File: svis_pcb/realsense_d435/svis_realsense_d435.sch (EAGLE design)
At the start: 14 parts, among them U1 MPU-6000QFN-24

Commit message: Adding libraries and packages.
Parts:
- removed C1: DNP (2.2nF), SparkFun-Capacitors:CAP0402-CAP
- removed C2, C3, C5, C6: 0.1uF, SparkFun-Capacitors:CAP0402-CAP
- removed C4: 2.2uF, SparkFun-Capacitors:CAP0402-CAP
- removed J2, J3: (no value), SparkFun-Connectors:M09
- removed JP1: MPU6050, SparkFun-Passives:JUMPER-PAD-2-NOYES_SILK
- removed JP2: JUMPER-SMT_3_NO_SILK, SparkFun-Jumpers:JUMPER-SMT_3_NO_SILK
- removed R1, R2: 4.7k, SparkFun-Resistors:RESISTOR0603
- removed U$2: TEENSY_3.2, Teensy_3_and_LC_Series_Boards_v1.1:TEENSY_3.1_DIL
- removed U1: MPU-6000QFN-24, SparkFun-Sensors:MPU-6000QFN-24
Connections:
- removed net 3.3V: C3.1, C4.1, C5.1, C6.1, R1.2, R2.2, U$2.3.3V, U1.CS, U1.VDD
- removed net C31_I0: J2.9, U$2.2
- removed net C31_IO2_RX: J2.5, U$2.1/TX1/T
- removed net C31_IO3_TX: J2.4, JP2.1, U$2.0/RX1/T
- removed net C31_O1: J2.8, U$2.4/CAN-RX-PWM
- removed net C32_I0: J3.9, U$2.3/CAN-TX/PWM
- removed net C32_IO2: J3.5, U$2.6/PWM
- removed net C32_IO3: J3.4, JP2.2
- removed net C32_IO3_T: JP2.3, U$2.7/RX3
- removed net C32_O1: J3.8, U$2.5/PWM
- removed net GND: C1.1, C2.1, C3.2, C4.2, C5.2, C6.2, J2.2, J2.6, J2.7, J3.2, J3.6, J3.7, JP1.1, U$2.AGND, U$2.GND, U1.AD0/SDO, U1.FSYNC, U1.GND
- removed net IMU2_INT: U$2.20/A6/PWM, U1.INT
- removed net N$7: C1.2, U1.CPOUT
- removed net N$8: JP1.2, U1.CLKIN
- removed net REGOUT: C2.2, U1.REGOUT
- removed net SCL: R1.1, U$2.19/A5/T/SCL0, U1.SCL/SCLK
- removed net SDA: R2.1, U$2.18/A4/T/SDA0, U1.SDA/SDI

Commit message: WIP.
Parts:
- added C1: 0.1uF, SparkFun-Capacitors:0.1UF-0402-16V-10%
- added U$1: TEENSY_3.0_DIL, teensy:TEENSY_3.0_DIL
- added U1: ICM-20689, svis:ICM-20689
- added U2: SM09B-SRSS-TB, svis:SM09B-SRSS-TB
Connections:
- new net 3.3V: U$1.3.3V, U1.VDD, U1.VDDIO
- new net GND: C1.1, U$1.AGND, U$1.GND, U1.EPX_PAD, U1.FSYNC, U1.GND
- new net IMU_INT: U1.INT
- new net N$1: C1.2, U1.REGOUT
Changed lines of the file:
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@@
 <setting verticaltext="up"/>
 </settings>
-<grid distance="0.05" unitdist="inch" unit="inch" style="lines" multiple="1" display="no" altdistance="0.025" altunitdist="inch" altunit="inch"/>
+<grid distance="0.1" unitdist="inch" unit="inch" style="lines" multiple="1" display="no" altdistance="0.01" altunitdist="inch" altunit="inch"/>
 <layers>
 <layer number="1" name="Top" color="4" fill="1" visible="no" active="no"/>
@@
 </classes>
 <parts>
+<part name="U1" library="svis" deviceset="ICM-20689" device=""/>
+<part name="U2" library="svis" deviceset="SM09B-SRSS-TB" device=""/>
+<part name="GND1" library="SparkFun-PowerSymbols" deviceset="GND" device=""/>
+<part name="SUPPLY1" library="SparkFun-PowerSymbols" deviceset="3.3V" device=""/>
+<part name="U$1" library="teensy" deviceset="TEENSY_3.0_DIL" device=""/>
+<part name="GND2" library="SparkFun-PowerSymbols" deviceset="GND" device=""/>
+<part name="SUPPLY2" library="SparkFun-PowerSymbols" deviceset="3.3V" device=""/>
+<part name="GND3" library="SparkFun-PowerSymbols" deviceset="GND" device=""/>
+<part name="C1" library="SparkFun-Capacitors" deviceset="0.1UF" device="-0402-16V-10%" value="0.1uF"/>
+<part name="GND4" library="SparkFun-PowerSymbols" deviceset="GND" device=""/>
 </parts>
 <sheets>
@@
 </plain>
 <instances>
+<instance part="U1" gate="G$1" x="63.5" y="50.8"/>
+<instance part="U2" gate="G$1" x="60.96" y="96.52"/>
+<instance part="GND1" gate="1" x="177.8" y="73.66"/>
+<instance part="SUPPLY1" gate="G$1" x="177.8" y="101.6"/>
+<instance part="U$1" gate="G$1" x="152.4" y="73.66"/>
+<instance part="GND2" gate="1" x="86.36" y="33.02"/>
+<instance part="SUPPLY2" gate="G$1" x="86.36" y="66.04"/>
+<instance part="GND3" gate="1" x="30.48" y="33.02"/>
+<instance part="C1" gate="G$1" x="101.6" y="48.26" rot="R180"/>
+<instance part="GND4" gate="1" x="101.6" y="38.1"/>
 </instances>
 <busses>
 </busses>
 <nets>
+<net name="GND" class="0">
+<segment>
+<pinref part="U$1" gate="G$1" pin="GND"/>
+<pinref part="GND1" gate="1" pin="GND"/>
+<wire x1="175.26" y1="93.98" x2="177.8" y2="93.98" width="0.1524" layer="91"/>
+<wire x1="177.8" y1="93.98" x2="177.8" y2="78.74" width="0.1524" layer="91"/>
+<pinref part="U$1" gate="G$1" pin="AGND"/>
+<wire x1="177.8" y1="78.74" x2="177.8" y2="76.2" width="0.1524" layer="91"/>
+<wire x1="175.26" y1="78.74" x2="177.8" y2="78.74" width="0.1524" layer="91"/>
+<junction x="177.8" y="78.74"/>
+</segment>
+<segment>
+<pinref part="U1" gate="G$1" pin="GND"/>
+<pinref part="GND2" gate="1" pin="GND"/>
+<wire x1="83.82" y1="40.64" x2="86.36" y2="40.64" width="0.1524" layer="91"/>
+<wire x1="86.36" y1="40.64" x2="86.36" y2="38.1" width="0.1524" layer="91"/>
+<pinref part="U1" gate="G$1" pin="EPX_PAD"/>
+<wire x1="86.36" y1="38.1" x2="86.36" y2="35.56" width="0.1524" layer="91"/>
+<wire x1="83.82" y1="38.1" x2="86.36" y2="38.1" width="0.1524" layer="91"/>
+<junction x="86.36" y="38.1"/>
+</segment>
+<segment>
+<pinref part="U1" gate="G$1" pin="FSYNC"/>
+<pinref part="GND3" gate="1" pin="GND"/>
+<wire x1="43.18" y1="55.88" x2="30.48" y2="55.88" width="0.1524" layer="91"/>
+<wire x1="30.48" y1="55.88" x2="30.48" y2="35.56" width="0.1524" layer="91"/>
+</segment>
+<segment>
+<pinref part="C1" gate="G$1" pin="1"/>
+<pinref part="GND4" gate="1" pin="GND"/>
+<wire x1="101.6" y1="43.18" x2="101.6" y2="40.64" width="0.1524" layer="91"/>
+</segment>
+</net>
+<net name="3.3V" class="0">
+<segment>
+<pinref part="U$1" gate="G$1" pin="3.3V"/>
+<pinref part="SUPPLY1" gate="G$1" pin="3.3V"/>
+<wire x1="175.26" y1="99.06" x2="177.8" y2="99.06" width="0.1524" layer="91"/>
+<wire x1="177.8" y1="99.06" x2="177.8" y2="101.6" width="0.1524" layer="91"/>
+</segment>
+<segment>
+<pinref part="SUPPLY2" gate="G$1" pin="3.3V"/>
+<wire x1="86.36" y1="66.04" x2="86.36" y2="63.5" width="0.1524" layer="91"/>
+<pinref part="U1" gate="G$1" pin="VDDIO"/>
+<wire x1="86.36" y1="63.5" x2="83.82" y2="63.5" width="0.1524" layer="91"/>
+<wire x1="86.36" y1="63.5" x2="86.36" y2="60.96" width="0.1524" layer="91"/>
+<pinref part="U1" gate="G$1" pin="VDD"/>
+<wire x1="86.36" y1="60.96" x2="83.82" y2="60.96" width="0.1524" layer="91"/>
+<junction x="86.36" y="63.5"/>
+</segment>
+</net>
+<net name="IMU_INT" class="0">
+<segment>
+<pinref part="U1" gate="G$1" pin="INT"/>
+<wire x1="83.82" y1="53.34" x2="86.36" y2="53.34" width="0.1524" layer="91"/>
+<label x="86.36" y="53.34" size="1.778" layer="95"/>
+</segment>
+</net>
+<net name="N$1" class="0">
+<segment>
+<pinref part="U1" gate="G$1" pin="REGOUT"/>
+<pinref part="C1" gate="G$1" pin="2"/>
+<wire x1="83.82" y1="55.88" x2="101.6" y2="55.88" width="0.1524" layer="91"/>
+<wire x1="101.6" y1="55.88" x2="101.6" y2="50.8" width="0.1524" layer="91"/>
+</segment>
+</net>
 </nets>
 </sheet>

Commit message: First cut at complete board.
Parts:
- removed U1: ICM-20689, svis:ICM-20689
- removed U2: SM09B-SRSS-TB, svis:SM09B-SRSS-TB
- added C2: 0.1uF, SparkFun-Capacitors:0.1UF-0603-25V-(+80/-20%)
- added C3: 2.2uF, SparkFun-Capacitors:2.2UF-0603-10V-20%
- added C4: 10nF, SparkFun-Capacitors:0.1UF-0603-25V-(+80/-20%)
- added CAM1, CAM2: SM09B-SRSS-TB, svis:SM09B-SRSS-TB
- added ICM20689: ICM-20689, svis:ICM-20689
- added R1, R2: 4.7k, SparkFun-Resistors:4.7KOHM-0603-1/10W-1%
- C1: value 0.1uF -> 0.47uF; device SparkFun-Capacitors:0.1UF-0402-16V-10% -> SparkFun-Capacitors:0.1UF-0603-25V-(+80/-20%)
- renumbered U$1 to TEENSY
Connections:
- new net CAM1_GND: CAM1.P$9
- new net CAM1_IO: CAM1.P$1, TEENSY.3/PWM
- new net CAM1_RX: CAM1.P$7, TEENSY.1/TX1/T
- new net CAM1_STROBE: CAM1.P$5, TEENSY.4/PWM
- new net CAM1_TRIGGER: CAM1.P$3, TEENSY.2
- new net CAM1_TX: CAM1.P$8, TEENSY.0/RX1/T
- new net CAM2_GND: CAM2.P$9
- new net CAM2_IO: CAM2.P$1, TEENSY.7/RX3
- new net CAM2_RX: CAM2.P$7, TEENSY.10/TX2/PWM
- new net CAM2_STROBE: CAM2.P$5, TEENSY.8/TX3
- new net CAM2_TRIGGER: CAM2.P$3, TEENSY.6/PWM
- new net CAM2_TX: CAM2.P$8, TEENSY.9/RX2/PWM
- new net IMU_SCL: ICM20689.SCL/SCLK, R1.1, TEENSY.19/A5/T/SCL
- new net IMU_SDA: ICM20689.SDA/SDI, R2.1, TEENSY.18/A4/T/SDA
- new net N$2: C2.2, C3.2, ICM20689.VDD
- net 3.3V: now also C2.1, C3.1, C4.2, ICM20689.NCS, ICM20689.VDDIO, R1.2, R2.2; no longer U1.VDD, U1.VDDIO
- net GND: now also C1.2, C4.1, CAM1.P$2, CAM1.P$4, CAM1.P$6, CAM2.P$2, CAM2.P$4, CAM2.P$6, ICM20689.AD0/SDO, ICM20689.EPX_PAD, ICM20689.FSYNC, ICM20689.GND; no longer C1.1, U1.EPX_PAD, U1.FSYNC, U1.GND
- net IMU_INT: now also ICM20689.INT, TEENSY.20/A6/PWM; no longer U1.INT
- net N$1: now also C1.1, ICM20689.REGOUT; no longer C1.2, U1.REGOUT
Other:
- moved on the sheet: C1

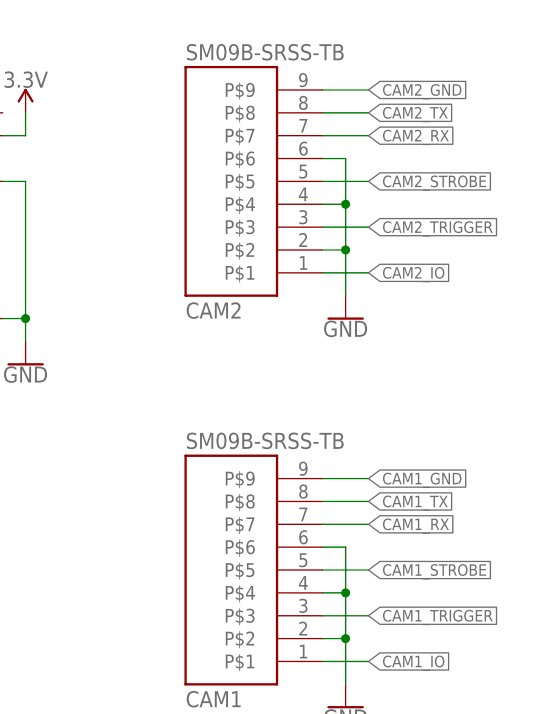
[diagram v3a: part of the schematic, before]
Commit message: Update design to pass DRC and ERC.
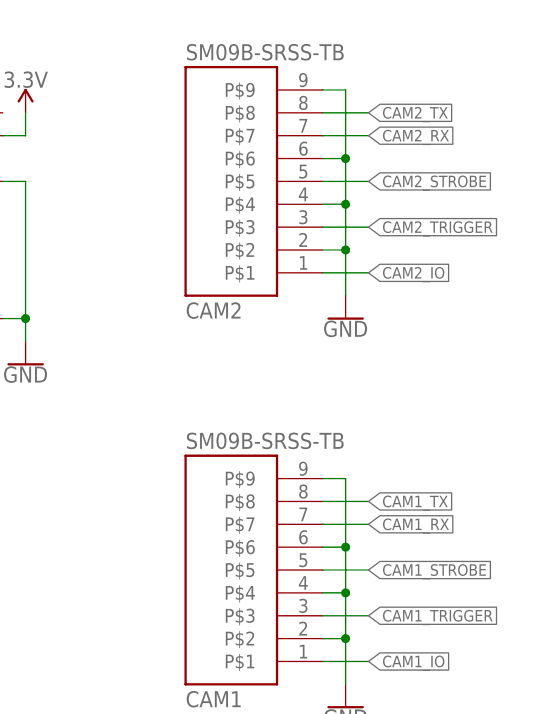
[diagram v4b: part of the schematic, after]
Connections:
- removed net CAM1_GND: CAM1.P$9
- removed net CAM2_GND: CAM2.P$9
- net GND: now also CAM1.P$9, CAM2.P$9
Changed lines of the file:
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@@
 <part name="SUPPLY1" library="SparkFun-PowerSymbols" deviceset="3.3V" device=""/>
 <part name="TEENSY" library="teensy" deviceset="TEENSY_3.0_DIL" device=""/>
-<part name="GND2" library="SparkFun-PowerSymbols" deviceset="GND" device=""/>
 <part name="SUPPLY2" library="SparkFun-PowerSymbols" deviceset="3.3V" device=""/>
 <part name="GND3" library="SparkFun-PowerSymbols" deviceset="GND" device=""/>
@@
 <part name="CAM2" library="svis" deviceset="SM09B-SRSS-TB" device=""/>
 <part name="GND8" library="SparkFun-PowerSymbols" deviceset="GND" device=""/>
+<part name="GND9" library="SparkFun-PowerSymbols" deviceset="GND" device=""/>
 </parts>
 <sheets>
@@
 <instance part="SUPPLY1" gate="G$1" x="177.8" y="101.6"/>
 <instance part="TEENSY" gate="G$1" x="152.4" y="73.66"/>
-<instance part="GND2" gate="1" x="78.74" y="35.56"/>
 <instance part="SUPPLY2" gate="G$1" x="93.98" y="78.74"/>
 <instance part="GND3" gate="1" x="17.78" y="53.34"/>
@@
 <instance part="CAM2" gate="G$1" x="200.66" y="93.98"/>
 <instance part="GND8" gate="1" x="213.36" y="78.74"/>
+<instance part="GND9" gate="1" x="78.74" y="35.56"/>
 </instances>
 <busses>
@@
 <wire x1="175.26" y1="78.74" x2="177.8" y2="78.74" width="0.1524" layer="91"/>
 <junction x="177.8" y="78.74"/>
-</segment>
-<segment>
-<pinref part="ICM20689" gate="G$1" pin="GND"/>
-<pinref part="GND2" gate="1" pin="GND"/>
-<wire x1="76.2" y1="43.18" x2="78.74" y2="43.18" width="0.1524" layer="91"/>
-<wire x1="78.74" y1="43.18" x2="78.74" y2="40.64" width="0.1524" layer="91"/>
-<pinref part="ICM20689" gate="G$1" pin="EPX_PAD"/>
-<wire x1="78.74" y1="40.64" x2="78.74" y2="38.1" width="0.1524" layer="91"/>
-<wire x1="76.2" y1="40.64" x2="78.74" y2="40.64" width="0.1524" layer="91"/>
-<junction x="78.74" y="40.64"/>
 </segment>
 <segment>
@@
 <wire x1="213.36" y1="53.34" x2="213.36" y2="48.26" width="0.1524" layer="91"/>
 <junction x="213.36" y="48.26"/>
+<pinref part="CAM1" gate="G$1" pin="P$9"/>
+<wire x1="210.82" y1="60.96" x2="213.36" y2="60.96" width="0.1524" layer="91"/>
+<wire x1="213.36" y1="60.96" x2="213.36" y2="53.34" width="0.1524" layer="91"/>
+<junction x="213.36" y="53.34"/>
 </segment>
 <segment>
@@
 <junction x="213.36" y="86.36"/>
 <junction x="213.36" y="91.44"/>
+<pinref part="CAM2" gate="G$1" pin="P$9"/>
+<wire x1="210.82" y1="104.14" x2="213.36" y2="104.14" width="0.1524" layer="91"/>
+<wire x1="213.36" y1="104.14" x2="213.36" y2="96.52" width="0.1524" layer="91"/>
+<junction x="213.36" y="96.52"/>
+</segment>
+<segment>
+<pinref part="ICM20689" gate="G$1" pin="EPX_PAD"/>
+<pinref part="GND9" gate="1" pin="GND"/>
+<wire x1="76.2" y1="40.64" x2="78.74" y2="40.64" width="0.1524" layer="91"/>
+<wire x1="78.74" y1="40.64" x2="78.74" y2="38.1" width="0.1524" layer="91"/>
+<pinref part="ICM20689" gate="G$1" pin="GND"/>
+<wire x1="76.2" y1="43.18" x2="78.74" y2="43.18" width="0.1524" layer="91"/>
+<wire x1="78.74" y1="43.18" x2="78.74" y2="40.64" width="0.1524" layer="91"/>
+<junction x="78.74" y="40.64"/>
 </segment>
 </net>
@@
 </segment>
 </net>
-<net name="CAM1_GND" class="0">
-<segment>
-<pinref part="CAM1" gate="G$1" pin="P$9"/>
-<wire x1="210.82" y1="60.96" x2="215.9" y2="60.96" width="0.1524" layer="91"/>
-<label x="215.9" y="60.96" size="1.27" layer="95" xref="yes"/>
-</segment>
-</net>
 <net name="CAM1_TX" class="0">
 <segment>
@@
 </segment>
 </net>
-<net name="CAM2_GND" class="0">
-<segment>
-<pinref part="CAM2" gate="G$1" pin="P$9"/>
-<wire x1="210.82" y1="104.14" x2="215.9" y2="104.14" width="0.1524" layer="91"/>
-<label x="215.9" y="104.14" size="1.27" layer="95" xref="yes"/>
-</segment>
-</net>

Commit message: Incorporate Samir's comments
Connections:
- removed net N$2: C2.2, C3.2, ICM20689.VDD
- net 3.3V: now also ICM20689.VDD
- net GND: now also C2.2, C3.2
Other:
- moved on the sheet: C1, C2, C3, C4, ICM20689, R1, R2
